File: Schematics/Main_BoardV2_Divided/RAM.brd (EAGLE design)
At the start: 167.6 x 178.7 mm, 46 parts

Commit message: Routd and Cams Created
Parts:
- moved RAM1:IC12 10.9 mm to (90.2, 94.0)
- moved RAM1:IC13 10.9 mm to (90.2, 68.6)
- moved RAM1:IC15 10.9 mm to (109.2, 41.9)
- moved RAM1:IC16 10.9 mm to (109.2, 15.2)
- moved RAM1:IC17 10.9 mm to (90.2, 41.9)
- moved RAM1:IC18 10.9 mm to (90.2, 15.2)
- moved RAM1:IC2 10.9 mm to (109.2, 94.0)
- moved RAM1:IC3 10.9 mm to (109.2, 68.6)
- moved RAM1:LED13 10.2 mm to (135.9, 165.1)
- moved RAM1:LED14 10.2 mm to (129.5, 165.1)
- moved RAM1:LED15 10.2 mm to (123.2, 165.1)
- moved RAM1:LED11 10.2 mm to (110.5, 165.1)
- moved RAM1:LED16 10.2 mm to (116.8, 165.1)
- moved RAM1:LED9 10.2 mm to (104.1, 165.1)
- moved RAM1:LED10 10.2 mm to (148.6, 165.1)
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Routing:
- net VCC: track 0.00 -> 490.5 mm
- net RAM1:N$40: track 0.00 -> 336.2 mm, vias 0 -> 1
- net RAM1:N$37: track 0.00 -> 299.2 mm, vias 0 -> 5
- net RAM1:N$36: track 0.00 -> 298.6 mm, vias 0 -> 2
- net RAM1:N$41: track 0.00 -> 293.4 mm, vias 0 -> 3
- net RAM1:N$44: track 0.00 -> 264.7 mm, vias 0 -> 2
- net RAM1:N$43: track 0.00 -> 243.3 mm, vias 0 -> 1
- net RAM1:N$42: track 0.00 -> 221.4 mm, vias 0 -> 5
- net |RAM_OUT: track 0.00 -> 214.5 mm, vias 0 -> 3
- net RAM1:N$45: track 0.00 -> 197.3 mm, vias 0 -> 8
- net SLC_ADDR: track 0.00 -> 182.7 mm, vias 0 -> 1
- net 8B_8: track 0.00 -> 174.5 mm, vias 0 -> 1
- net CLR: track 0.00 -> 171.0 mm
- net CLK: track 0.00 -> 163.7 mm, vias 0 -> 1
- net 8B_7: track 0.00 -> 163.2 mm, vias 0 -> 1
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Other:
- board size 167.6 x 178.7 mm -> 157.5 x 171.1 mm
- board text added: "16Bit Bus"
- board text added: "8Bit Buffer"
- board text added: "A/M Select"
- board text added: "Address"
- board text added: "Control Signals"
- board text added: "Manual Inputs"

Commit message: Visual Improvments
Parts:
- RAM1:S2: device switch:320-916 -> TE_4-1825136-5:TE_4-1825136-5
- RAM1:SV1, SV22: device con-lstb:MA08-2 -> pinhead:2X08
- SV16: device con-lstb:MA08-1 -> pinhead:1X08
- SV27: device con-lstb:MA04-1 -> pinhead:1X04
- turned RAM1:S2 to 270 degrees
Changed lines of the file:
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@@
 <drawing>
 <settings>
-<setting alwaysvectorfont="no"/>
+<setting alwaysvectorfont="yes"/>
 <setting verticaltext="up"/>
 </settings>
@@
 </layers>
 <board>
-<fusionsync huburn="a.cGVyc29uYWw6dWUyYzAxZDJj" projecturn="a.cGVyc29uYWw6dWUyYzAxZDJjIzIwMTkwNTA1MTkyMDg5NTI2" f3durn="urn:adsk.wipprod:dm.lineage:JFIK4NUQTn-YI1dwVml-6w" pcbguid="fcba0669-bcd8-4e06-9528-1b6a2dc584fb" lastpulledtime="" lastsyncedchangeguid="e137c6dc-be67-3cc7-ce79-9ef8c7ffbb3e"/>
+<fusionsync huburn="a.cGVyc29uYWw6dWUyYzAxZDJj" projecturn="a.cGVyc29uYWw6dWUyYzAxZDJjIzIwMTkwNTA1MTkyMDg5NTI2" f3durn="urn:adsk.wipprod:dm.lineage:JFIK4NUQTn-YI1dwVml-6w" pcbguid="fcba0669-bcd8-4e06-9528-1b6a2dc584fb" lastpulledtime="" lastsyncedchangeguid="ee053d0c-f900-aa73-f894-efc479de773e"/>
 <plain>
 <wire x1="0" y1="1.27" x2="157.46" y2="1.27" width="0" layer="20"/>
@@
 <attribute name="VALUE" x="105.41" y="156.21" size="0.9906" layer="27" ratio="10" rot="R90"/>
 </element>
-<element name="RAM1:S2" library="switch" library_urn="urn:adsk.eagle:library:380" package="320-916" package3d_urn="urn:adsk.eagle:package:27678/1" value="" x="10.16" y="161.29" smashed="yes">
-<attribute name="NAME" x="10.16" y="161.29" size="1.778" layer="25" ratio="10"/>
-<attribute name="VALUE" x="10.16" y="161.29" size="1.778" layer="27" ratio="10"/>
+<element name="RAM1:S2" library="TE_4-1825136-5" package="TE_4-1825136-5" package3d_urn="urn:adsk.eagle:package:12106955/2" value="" x="10.16" y="161.29" smashed="yes" rot="R270">
+<attribute name="NAME" x="11.43" y="161.29" size="1.778" layer="25" ratio="10" rot="R270"/>
+<attribute name="VALUE" x="10.16" y="161.29" size="1.778" layer="27" ratio="10" rot="R270"/>
 </element>
 <element name="RAM1:V1" library="74ttl-din" library_urn="urn:adsk.eagle:library:84" package="DIL14" package3d_urn="urn:adsk.eagle:package:16407/2" value="7409N" x="64.77" y="82.55" smashed="yes" rot="R270">
@@
 <attribute name="VALUE" x="64.77" y="82.55" size="1.27" layer="27" ratio="10" rot="R270"/>
 </element>
-<element name="SV16" library="con-lstb" library_urn="urn:adsk.eagle:library:162" package="MA08-1" package3d_urn="urn:adsk.eagle:package:8343/1" value="" x="148.59" y="82.55" smashed="yes" rot="R270">
+<element name="SV16" library="pinhead" library_urn="urn:adsk.eagle:library:325" package="1X08" package3d_urn="urn:adsk.eagle:package:22409/2" value="" x="148.59" y="82.55" smashed="yes" rot="R270">
 <attribute name="MF" value="" x="148.59" y="82.55" size="1.778" layer="27" rot="R270" display="off"/>
 <attribute name="MPN" value="" x="148.59" y="82.55" size="1.778" layer="27" rot="R270" display="off"/>
-<attribute name="NAME" x="148.59" y="82.55" size="1.27" layer="25" ratio="10" rot="R270"/>
+<attribute name="NAME" x="148.59" y="83.82" size="1.27" layer="25" ratio="10" rot="R270"/>
 <attribute name="OC_FARNELL" value="unknown" x="148.59" y="82.55" size="1.778" layer="27" rot="R270" display="off"/>
 <attribute name="OC_NEWARK" value="unknown" x="148.59" y="82.55" size="1.778" layer="27" rot="R270" display="off"/>
 <attribute name="VALUE" x="148.59" y="82.55" size="1.27" layer="27" ratio="10" rot="R270"/>
 </element>
-<element name="SV22" library="con-lstb" library_urn="urn:adsk.eagle:library:162" package="MA08-2" package3d_urn="urn:adsk.eagle:package:8335/1" value="" x="147.32" y="29.21" smashed="yes" rot="R90">
+<element name="SV22" library="pinhead" library_urn="urn:adsk.eagle:library:325" package="2X08" package3d_urn="urn:adsk.eagle:package:22481/2" value="" x="147.32" y="29.21" smashed="yes" rot="R90">
 <attribute name="MF" value="" x="147.32" y="29.21" size="1.778" layer="27" rot="R90" display="off"/>
 <attribute name="MPN" value="" x="147.32" y="29.21" size="1.778" layer="27" rot="R90" display="off"/>
-<attribute name="NAME" x="147.32" y="29.21" size="1.27" layer="25" ratio="10" rot="R90"/>
+<attribute name="NAME" x="147.32" y="30.48" size="1.27" layer="25" ratio="10" rot="R90"/>
 <attribute name="OC_FARNELL" value="unknown" x="147.32" y="29.21" size="1.778" layer="27" rot="R90" display="off"/>
 <attribute name="OC_NEWARK" value="unknown" x="147.32" y="29.21" size="1.778" layer="27" rot="R90" display="off"/>
 <attribute name="VALUE" x="147.32" y="29.21" size="1.27" layer="27" ratio="10" rot="R90"/>
 </element>
-<element name="SV27" library="con-lstb" library_urn="urn:adsk.eagle:library:162" package="MA04-1" package3d_urn="urn:adsk.eagle:package:8337/1" value="" x="12.7" y="123.19" smashed="yes" rot="R270">
+<element name="SV27" library="pinhead" library_urn="urn:adsk.eagle:library:325" package="1X04" package3d_urn="urn:adsk.eagle:package:22407/2" value="" x="12.7" y="123.19" smashed="yes" rot="R270">
 <attribute name="MF" value="" x="12.7" y="123.19" size="1.778" layer="27" rot="R270" display="off"/>
 <attribute name="MPN" value="" x="12.7" y="123.19" size="1.778" layer="27" rot="R270" display="off"/>
@@
 <attribute name="VALUE" x="15.875" y="139.7" size="1.27" layer="27" rot="R90"/>
 </element>
-<element name="RAM1:SV1" library="con-lstb" library_urn="urn:adsk.eagle:library:162" package="MA08-2" package3d_urn="urn:adsk.eagle:package:8335/1" value="" x="10.16" y="71.12" smashed="yes" rot="R90">
+<element name="RAM1:SV1" library="pinhead" library_urn="urn:adsk.eagle:library:325" package="2X08" package3d_urn="urn:adsk.eagle:package:22481/2" value="" x="10.16" y="71.12" smashed="yes" rot="R90">
 <attribute name="MF" value="" x="10.16" y="71.12" size="1.778" layer="27" rot="R90" display="off"/>
 <attribute name="MPN" value="" x="10.16" y="71.12" size="1.778" layer="27" rot="R90" display="off"/>
@@
 <wire x1="10.3759" y1="157.0863" x2="10.3759" y2="156.3624" width="0.254" layer="1"/>
 <wire x1="12.7889" y1="143.5735" x2="12.7" y2="143.51" width="0.254" layer="1"/>
-<wire x1="10.3759" y1="157.0863" x2="10.16" y2="157.2768" width="0.254" layer="1"/>
+<wire x1="10.3759" y1="157.0863" x2="10.16" y2="156.591" width="0.254" layer="1"/>
 <wire x1="35.4711" y1="141.1605" x2="34.9885" y2="141.1605" width="0.254" layer="1"/>
 <wire x1="34.9885" y1="141.1605" x2="34.5059" y2="141.1605" width="0.254" layer="1"/>
@@
 <wire x1="30.6451" y1="102.7938" x2="30.48" y2="102.87" width="0.254" layer="1"/>
 <wire x1="30.4038" y1="80.1116" x2="30.48" y2="80.01" width="0.254" layer="1"/>
-<wire x1="10.8585" y1="161.1884" x2="10.3759" y2="161.1884" width="0.254" layer="16"/>
-<wire x1="12.7889" y1="159.258" x2="10.8585" y2="161.1884" width="0.254" layer="16"/>
+<wire x1="10.0584" y1="160.5915" x2="10.0584" y2="161.0741" width="0.254" layer="16"/>
+<wire x1="12.7889" y1="159.258" x2="10.0584" y2="160.5915" width="0.254" layer="16"/>
 <wire x1="13.0302" y1="159.258" x2="12.7889" y2="159.258" width="0.254" layer="16"/>
 <wire x1="30.6451" y1="141.6431" x2="13.0302" y2="159.258" width="0.254" layer="16"/>
 <wire x1="30.6451" y1="103.0351" x2="30.6451" y2="141.6431" width="0.254" layer="16"/>
-<wire x1="10.3759" y1="161.1884" x2="10.16" y2="161.29" width="0.254" layer="16"/>
+<wire x1="10.0584" y1="161.0741" x2="10.16" y2="161.29" width="0.254" layer="16"/>
 <wire x1="30.6451" y1="103.0351" x2="30.48" y2="102.87" width="0.254" layer="16"/>
 </signal>

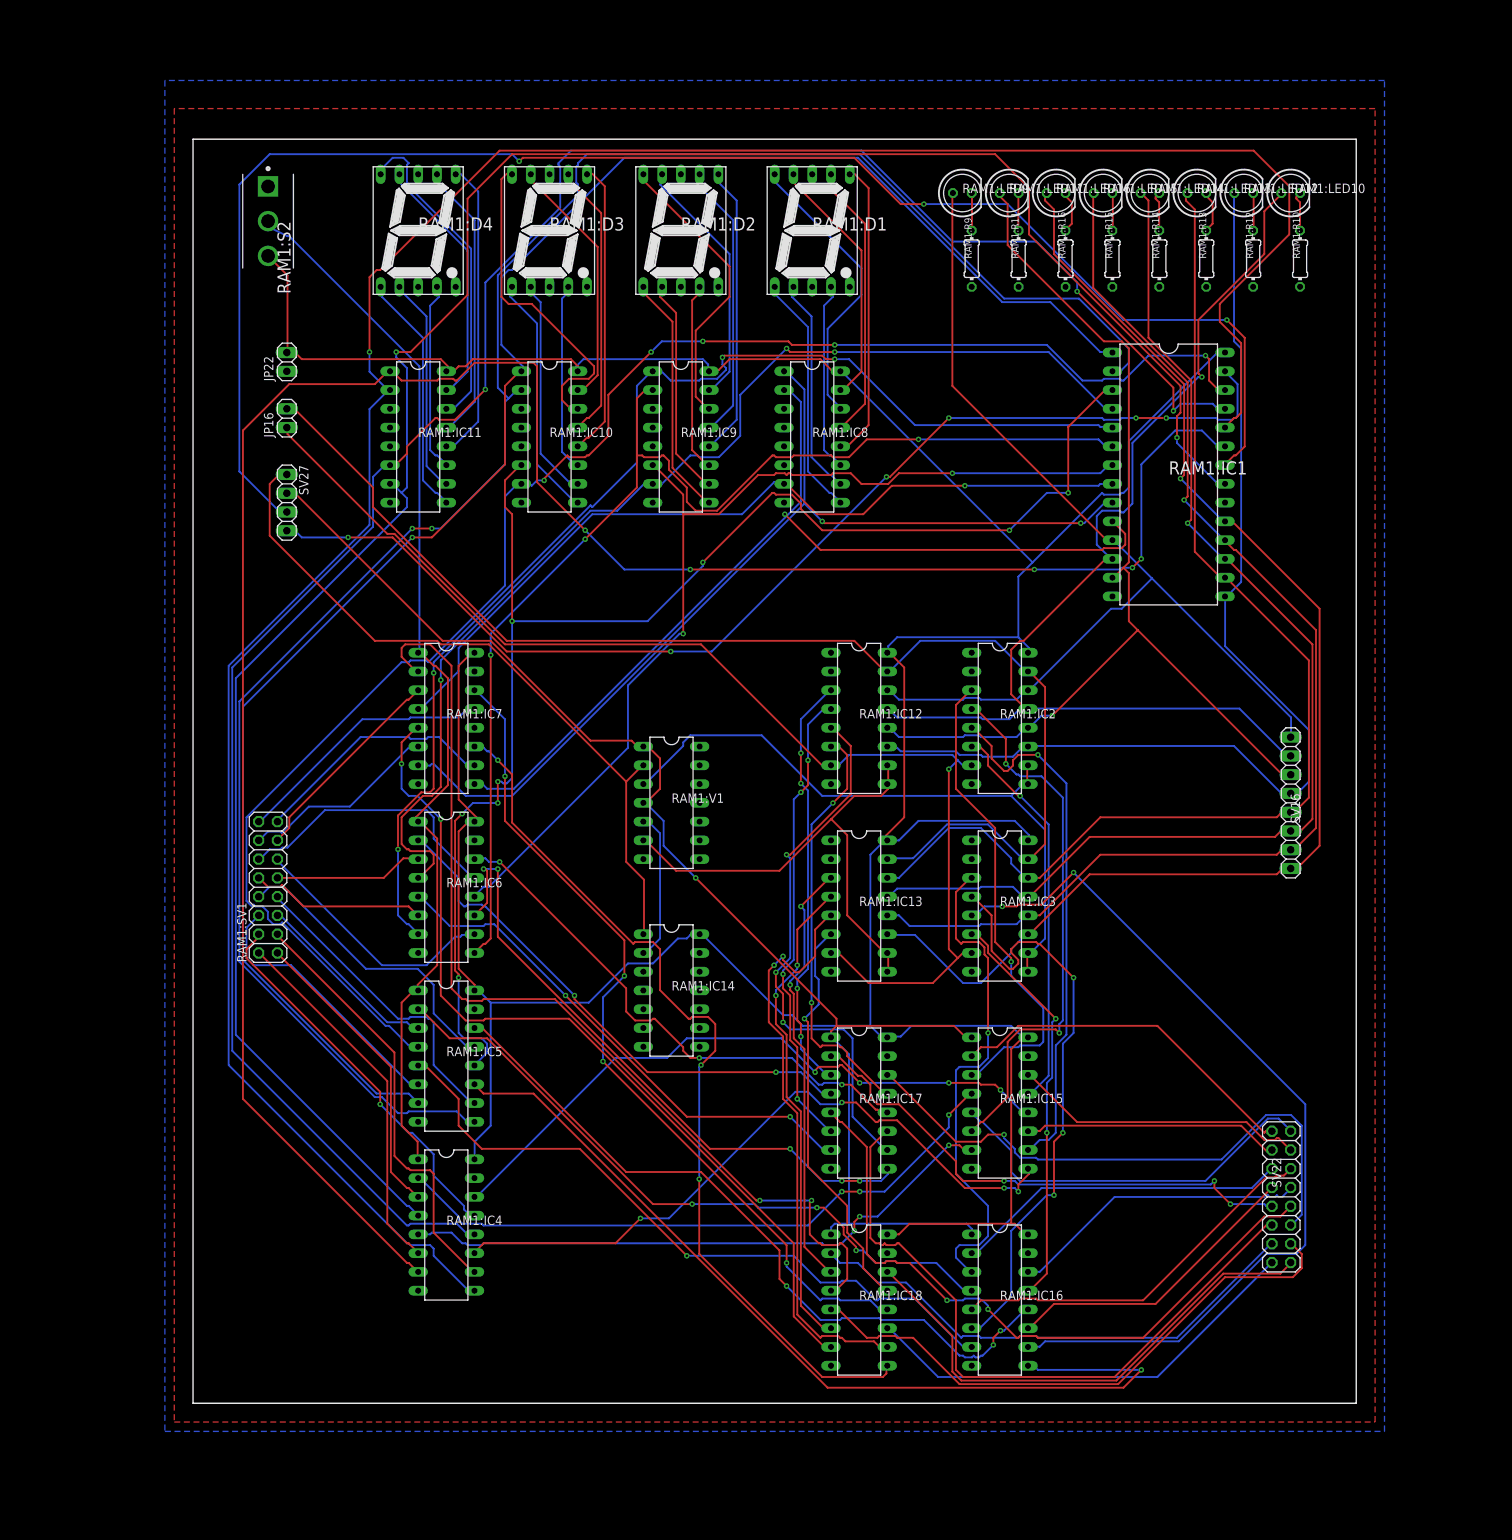
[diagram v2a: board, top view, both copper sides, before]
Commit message: Microcode Added and Ram Updated
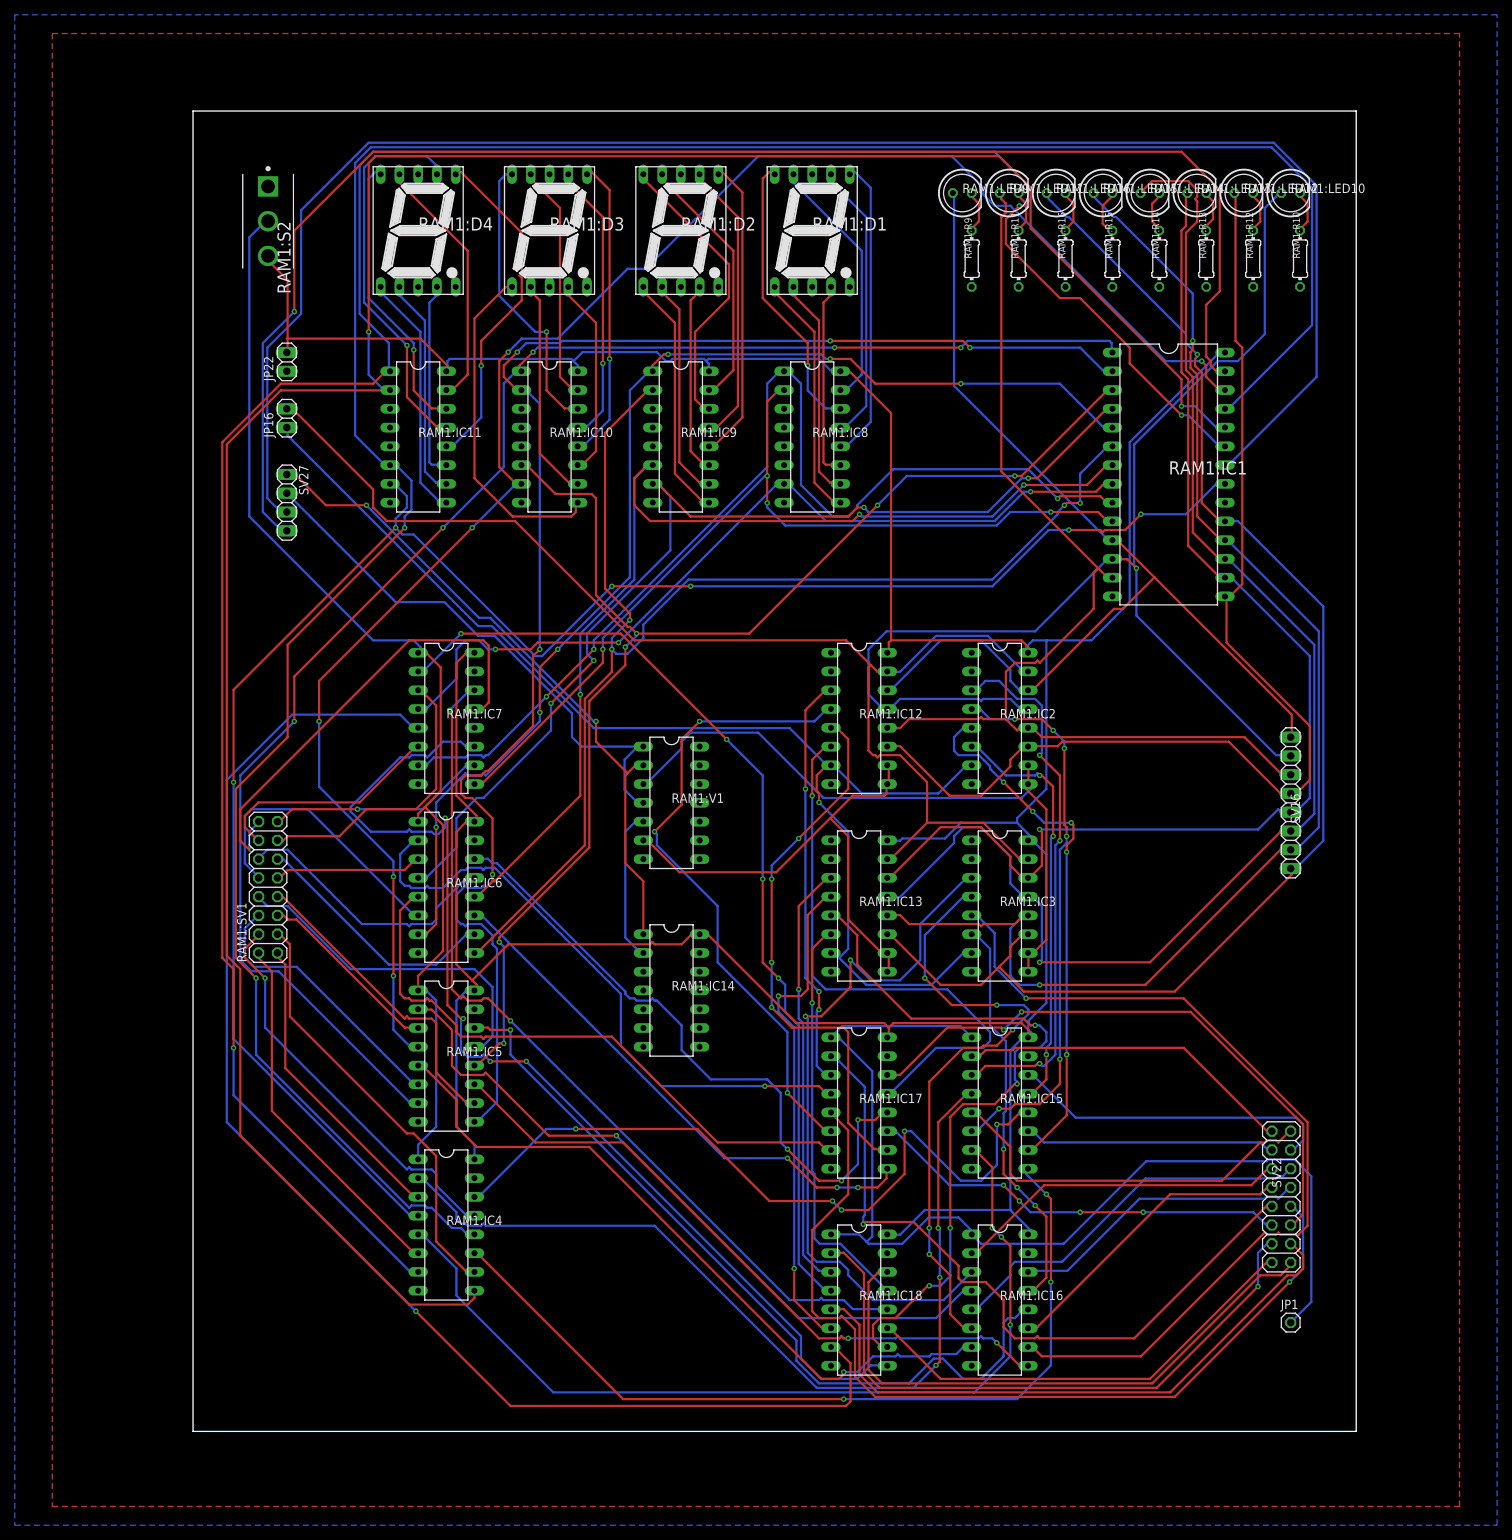
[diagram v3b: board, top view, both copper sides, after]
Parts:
- added JP1: (no value), pinhead:1X01
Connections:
- new net NNOW2: JP1.1, RAM1:IC15.1, RAM1:IC16.1, RAM1:IC17.1, RAM1:IC18.1
- net SLC_ADDR: no longer RAM1:IC15.1, RAM1:IC16.1, RAM1:IC17.1, RAM1:IC18.1
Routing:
- net NNOW2: track 0.00 -> 146.6 mm
- net SLC_ADDR: track 182.7 -> 75.0 mm, vias 1 -> 0
- net RAM1:N$17: track 119.0 -> 186.1 mm, vias 2 -> 1
- net RAM1:N$44: track 264.7 -> 208.8 mm, vias 2 -> 5
- net RAM1:N$41: track 293.4 -> 343.6 mm, vias 3 -> 2
- net RAM1:N$36: track 298.6 -> 250.5 mm, vias 2 -> 6
- net |RAM_WRITE: track 155.9 -> 203.0 mm, vias 6 -> 1
- net RAM1:N$5: track 82.5 -> 123.7 mm
- net RAM1:N$4: track 86.2 -> 123.3 mm
- net N$76: track 92.1 -> 57.4 mm, vias 0 -> 4
- net RAM1:N$10: track 123.9 -> 91.6 mm, vias 1 -> 2
- net RAM1:N$43: track 243.3 -> 212.0 mm, vias 1 -> 5
- net N$75: track 91.6 -> 121.7 mm, vias 2 -> 1
- net RAM1:N$83: track 67.4 -> 96.5 mm, vias 1 -> 2
- net 8B_6: track 158.3 -> 187.4 mm
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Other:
- board size 157.5 x 171.1 mm -> 157.5 x 178.7 mm
